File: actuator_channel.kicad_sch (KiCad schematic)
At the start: 1 part

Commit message: исправлены метки
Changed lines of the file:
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@@
 		(instances
 			(project "Untitled"
-				(path "/fcc635d1-682a-4f5e-8a7f-d7e6794df01b"
+				(path "/7d251458-e0b3-4fe3-bf23-623a219baaaa"
 					(reference "U")
 					(unit 1)
@@
 	)
 	(label "GND"
-		(at 48.26 30.48 0)
+		(at 48.26 34.29 270)
 		(effects
 			(font

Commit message: fix writer
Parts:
- removed U: DRV8871 H-мост, symbol Driver_Motor:DRV8871DDA
- added C1, C2: 100nF, symbol Device:C
- added R1: 33k, symbol Device:R
- added R2: 10k, symbol Device:R
- added R3: 20k, symbol Device:R
- added U1: DRV8871 H-мост, symbol Driver_Motor:DRV8871DDA
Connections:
- net FB: now also C2.1, R2.2, R3.1
- net FB_RAW: now also R2.1
- net GND: now also C1.1, C1.2, C2.2, R3.2, U1.1 (GND), U1.5 (VM), U1.7 (GND), U1.9 (GND)
- net IN2: now also U1.2 (IN2)
- new net: R1.1, U1.4 (ILIM)
- new net IN1: U1.3 (IN1)
- new net MOTOR_A: U1.6 (OUT1)
- new net MOTOR_B: U1.8 (OUT2)

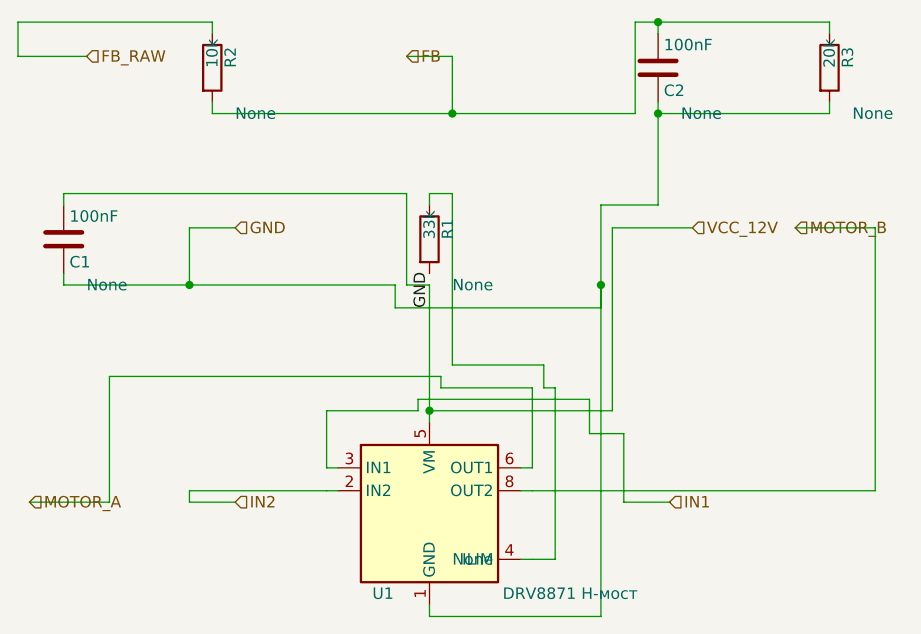
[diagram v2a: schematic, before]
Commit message: реализована 2я занятость клетки
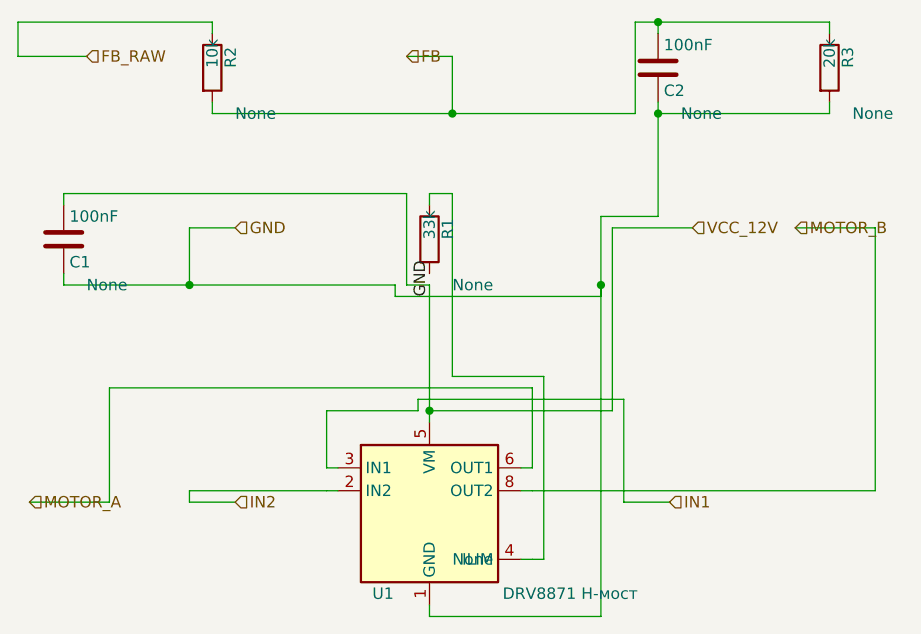
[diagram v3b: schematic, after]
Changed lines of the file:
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@@
 		(instances
 			(project "Untitled"
-				(path "/5363cd59-61ce-4477-bfeb-caaeda29f830"
+				(path "/a4230c37-048a-4d4e-aa82-9745794e2b61"
 					(reference "U1")
 					(unit 1)
@@
 		(instances
 			(project "Untitled"
-				(path "/5363cd59-61ce-4477-bfeb-caaeda29f830"
+				(path "/a4230c37-048a-4d4e-aa82-9745794e2b61"
 					(reference "C1")
 					(unit 1)
@@
 		(instances
 			(project "Untitled"
-				(path "/5363cd59-61ce-4477-bfeb-caaeda29f830"
+				(path "/a4230c37-048a-4d4e-aa82-9745794e2b61"
 					(reference "R1")
 					(unit 1)
@@
 		(instances
 			(project "Untitled"
-				(path "/5363cd59-61ce-4477-bfeb-caaeda29f830"
+				(path "/a4230c37-048a-4d4e-aa82-9745794e2b61"
 					(reference "R2")
 					(unit 1)
@@
 		(instances
 			(project "Untitled"
-				(path "/5363cd59-61ce-4477-bfeb-caaeda29f830"
+				(path "/a4230c37-048a-4d4e-aa82-9745794e2b61"
 					(reference "R3")
 					(unit 1)
@@
 		(instances
 			(project "Untitled"
-				(path "/5363cd59-61ce-4477-bfeb-caaeda29f830"
+				(path "/a4230c37-048a-4d4e-aa82-9745794e2b61"
 					(reference "C2")
 					(unit 1)
@@
 	(wire
 		(pts
-			(xy 67.31 68.58) (xy 67.31 22.86)
-		)
-		(stroke
-			(width 0)
-			(type default)
-		)
-	)
-	(wire
-		(pts
-			(xy 67.31 22.86) (xy 73.66 22.86)
-		)
-		(stroke
-			(width 0)
-			(type default)
-		)
-	)
-	(wire
-		(pts
-			(xy 73.66 22.86) (xy 73.66 12.7)
+			(xy 67.31 68.58) (xy 67.31 24.13)
+		)
+		(stroke
+			(width 0)
+			(type default)
+		)
+	)
+	(wire
+		(pts
+			(xy 67.31 24.13) (xy 73.66 24.13)
+		)
+		(stroke
+			(width 0)
+			(type default)
+		)
+	)
+	(wire
+		(pts
+			(xy 73.66 24.13) (xy 73.66 12.7)
 		)
 		(stroke
@@
 	(wire
 		(pts
-			(xy 44.45 31.75) (xy 44.45 34.29)
-		)
-		(stroke
-			(width 0)
-			(type default)
-		)
-	)
-	(wire
-		(pts
-			(xy 44.45 34.29) (xy 67.31 34.29)
-		)
-		(stroke
-			(width 0)
-			(type default)
-		)
-	)
-	(wire
-		(pts
-			(xy 67.31 34.29) (xy 67.31 31.75)
+			(xy 44.45 31.75) (xy 44.45 33.02)
+		)
+		(stroke
+			(width 0)
+			(type default)
+		)
+	)
+	(wire
+		(pts
+			(xy 44.45 33.02) (xy 67.31 33.02)
+		)
+		(stroke
+			(width 0)
+			(type default)
+		)
+	)
+	(wire
+		(pts
+			(xy 67.31 33.02) (xy 67.31 31.75)
 		)
 		(stroke
@@
 	(wire
 		(pts
-			(xy 46.99 44.45) (xy 66.04 44.45)
-		)
-		(stroke
-			(width 0)
-			(type default)
-		)
-	)
-	(wire
-		(pts
-			(xy 66.04 44.45) (xy 66.04 48.26)
-		)
-		(stroke
-			(width 0)
-			(type default)
-		)
-	)
-	(wire
-		(pts
-			(xy 66.04 48.26) (xy 69.85 48.26)
-		)
-		(stroke
-			(width 0)
-			(type default)
-		)
-	)
-	(wire
-		(pts
-			(xy 69.85 48.26) (xy 69.85 55.88)
+			(xy 46.99 44.45) (xy 69.85 44.45)
+		)
+		(stroke
+			(width 0)
+			(type default)
+		)
+	)
+	(wire
+		(pts
+			(xy 69.85 44.45) (xy 69.85 55.88)
 		)
 		(stroke
@@
 	(wire
 		(pts
-			(xy 59.69 43.18) (xy 49.53 43.18)
-		)
-		(stroke
-			(width 0)
-			(type default)
-		)
-	)
-	(wire
-		(pts
-			(xy 49.53 43.18) (xy 49.53 41.91)
-		)
-		(stroke
-			(width 0)
-			(type default)
-		)
-	)
-	(wire
-		(pts
-			(xy 49.53 41.91) (xy 12.7 41.91)
-		)
-		(stroke
-			(width 0)
-			(type default)
-		)
-	)
-	(wire
-		(pts
-			(xy 12.7 41.91) (xy 12.7 55.88)
+			(xy 59.69 43.18) (xy 12.7 43.18)
+		)
+		(stroke
+			(width 0)
+			(type default)
+		)
+	)
+	(wire
+		(pts
+			(xy 12.7 43.18) (xy 12.7 55.88)
 		)
 		(stroke
@@
 	(wire
 		(pts
-			(xy 59.69 62.23) (xy 62.23 62.23)
-		)
-		(stroke
-			(width 0)
-			(type default)
-		)
-	)
-	(wire
-		(pts
-			(xy 62.23 62.23) (xy 62.23 43.18)
-		)
-		(stroke
-			(width 0)
-			(type default)
-		)
-	)
-	(wire
-		(pts
-			(xy 62.23 43.18) (xy 60.96 43.18)
-		)
-		(stroke
-			(width 0)
-			(type default)
-		)
-	)
-	(wire
-		(pts
-			(xy 60.96 43.18) (xy 60.96 40.64)
-		)
-		(stroke
-			(width 0)
-			(type default)
-		)
-	)
-	(wire
-		(pts
-			(xy 60.96 40.64) (xy 50.8 40.64)
-		)
-		(stroke
-			(width 0)
-			(type default)
-		)
-	)
-	(wire
-		(pts
-			(xy 50.8 40.64) (xy 50.8 21.59)
+			(xy 59.69 62.23) (xy 60.96 62.23)
+		)
+		(stroke
+			(width 0)
+			(type default)
+		)
+	)
+	(wire
+		(pts
+			(xy 60.96 62.23) (xy 60.96 41.91)
+		)
+		(stroke
+			(width 0)
+			(type default)
+		)
+	)
+	(wire
+		(pts
+			(xy 60.96 41.91) (xy 50.8 41.91)
+		)
+		(stroke
+			(width 0)
+			(type default)
+		)
+	)
+	(wire
+		(pts
+			(xy 50.8 41.91) (xy 50.8 21.59)
 		)
 		(stroke
@@
 	)
 	(label "GND"
-		(at 48.26 34.29 270)
+		(at 48.26 33.02 270)
 		(effects
 			(font

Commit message: фильтр клеток для Т если там пересечение
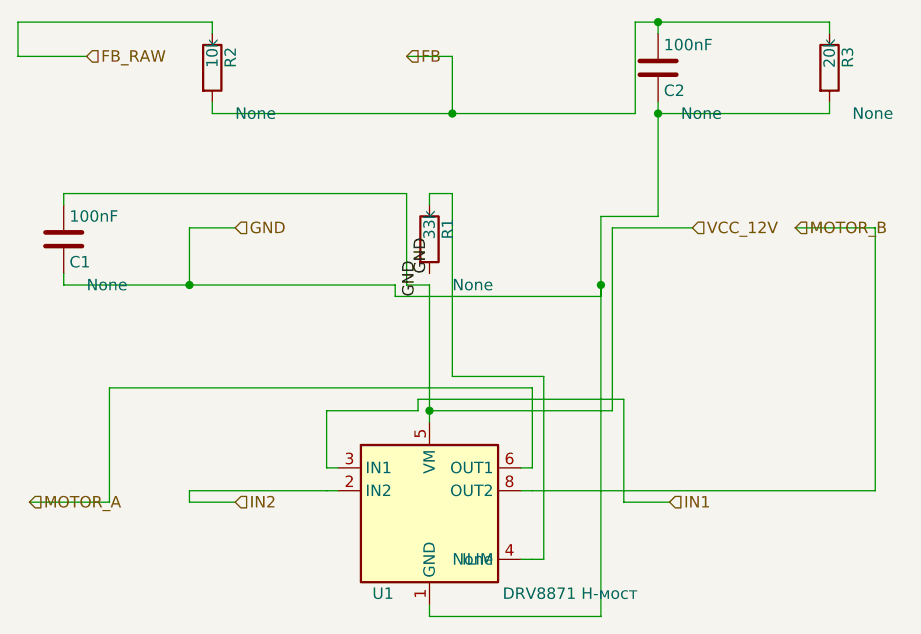
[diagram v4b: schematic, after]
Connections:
- net GND: now also R1.2; no longer C1.1, U1.5 (VM)
- new net VCC_12V: C1.1, U1.5 (VM)
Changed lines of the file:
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@@
 		(instances
 			(project "Untitled"
-				(path "/a4230c37-048a-4d4e-aa82-9745794e2b61"
+				(path "/f13d2b60-b3dd-4fee-9648-3bccc14a03e5"
 					(reference "U1")
 					(unit 1)
@@
 		(instances
 			(project "Untitled"
-				(path "/a4230c37-048a-4d4e-aa82-9745794e2b61"
+				(path "/f13d2b60-b3dd-4fee-9648-3bccc14a03e5"
 					(reference "C1")
 					(unit 1)
@@
 		(instances
 			(project "Untitled"
-				(path "/a4230c37-048a-4d4e-aa82-9745794e2b61"
+				(path "/f13d2b60-b3dd-4fee-9648-3bccc14a03e5"
 					(reference "R1")
 					(unit 1)
@@
 		(instances
 			(project "Untitled"
-				(path "/a4230c37-048a-4d4e-aa82-9745794e2b61"
+				(path "/f13d2b60-b3dd-4fee-9648-3bccc14a03e5"
 					(reference "R2")
 					(unit 1)
@@
 		(instances
 			(project "Untitled"
-				(path "/a4230c37-048a-4d4e-aa82-9745794e2b61"
+				(path "/f13d2b60-b3dd-4fee-9648-3bccc14a03e5"
 					(reference "R3")
 					(unit 1)
@@
 		(instances
 			(project "Untitled"
-				(path "/a4230c37-048a-4d4e-aa82-9745794e2b61"
+				(path "/f13d2b60-b3dd-4fee-9648-3bccc14a03e5"
 					(reference "C2")
 					(unit 1)
@@
 	)
 	(label "GND"
-		(at 48.26 33.02 270)
+		(at 48.26 30.48 270)
 		(effects
 			(font
+				(size 1.27 1.27)
+			)
+			(justify left bottom)
+		)
+	)
+	(label "GND"
+		(at 46.99 33.02 270)
+		(effects
+			(font

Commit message: fic placer for small schemes
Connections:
- net ILIM: now reaches R1.1, U1.4 (ILIM)
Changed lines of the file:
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@@
 		(instances
 			(project "Untitled"
-				(path "/f13d2b60-b3dd-4fee-9648-3bccc14a03e5"
+				(path "/56d967d8-6018-41d7-94fb-71f4db0aa129"
 					(reference "U1")
 					(unit 1)
@@
 		(instances
 			(project "Untitled"
-				(path "/f13d2b60-b3dd-4fee-9648-3bccc14a03e5"
+				(path "/56d967d8-6018-41d7-94fb-71f4db0aa129"
 					(reference "C1")
 					(unit 1)
@@
 		(instances
 			(project "Untitled"
-				(path "/f13d2b60-b3dd-4fee-9648-3bccc14a03e5"
+				(path "/56d967d8-6018-41d7-94fb-71f4db0aa129"
 					(reference "R1")
 					(unit 1)
@@
 		(instances
 			(project "Untitled"
-				(path "/f13d2b60-b3dd-4fee-9648-3bccc14a03e5"
+				(path "/56d967d8-6018-41d7-94fb-71f4db0aa129"
 					(reference "R2")
 					(unit 1)
@@
 		(instances
 			(project "Untitled"
-				(path "/f13d2b60-b3dd-4fee-9648-3bccc14a03e5"
+				(path "/56d967d8-6018-41d7-94fb-71f4db0aa129"
 					(reference "R3")
 					(unit 1)
@@
 		(instances
 			(project "Untitled"
-				(path "/f13d2b60-b3dd-4fee-9648-3bccc14a03e5"
+				(path "/56d967d8-6018-41d7-94fb-71f4db0aa129"
 					(reference "C2")
 					(unit 1)
@@
 		(effects
 			(font
+				(size 1.27 1.27)
+			)
+			(justify left bottom)
+		)
+	)
+	(label "ILIM"
+		(at 60.96 62.23 0.0000)
+		(effects
+			(font

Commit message: all unit test pass
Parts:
- C1, C2: value 100nF -> 100n
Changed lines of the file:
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@@
 		(instances
 			(project "Untitled"
-				(path "/56d967d8-6018-41d7-94fb-71f4db0aa129"
+				(path "/de9cf979-a599-4356-b152-ff3f043da01c"
 					(reference "U1")
 					(unit 1)
@@
 			)
 		)
-		(property "Value" "100nF"
+		(property "Value" "100n"
 			(at 8.255 24.13 0.0000)
 			(effects
@@
 		(instances
 			(project "Untitled"
-				(path "/56d967d8-6018-41d7-94fb-71f4db0aa129"
+				(path "/de9cf979-a599-4356-b152-ff3f043da01c"
 					(reference "C1")
 					(unit 1)
@@
 		(instances
 			(project "Untitled"
-				(path "/56d967d8-6018-41d7-94fb-71f4db0aa129"
+				(path "/de9cf979-a599-4356-b152-ff3f043da01c"
 					(reference "R1")
 					(unit 1)
@@
 		(instances
 			(project "Untitled"
-				(path "/56d967d8-6018-41d7-94fb-71f4db0aa129"
+				(path "/de9cf979-a599-4356-b152-ff3f043da01c"
 					(reference "R2")
 					(unit 1)
@@
 		(instances
 			(project "Untitled"
-				(path "/56d967d8-6018-41d7-94fb-71f4db0aa129"
+				(path "/de9cf979-a599-4356-b152-ff3f043da01c"
 					(reference "R3")
 					(unit 1)
@@
 			)
 		)
-		(property "Value" "100nF"
+		(property "Value" "100n"
 			(at 74.295 5.08 0.0000)
 			(effects
@@
 		(instances
 			(project "Untitled"
-				(path "/56d967d8-6018-41d7-94fb-71f4db0aa129"
+				(path "/de9cf979-a599-4356-b152-ff3f043da01c"
 					(reference "C2")
 					(unit 1)

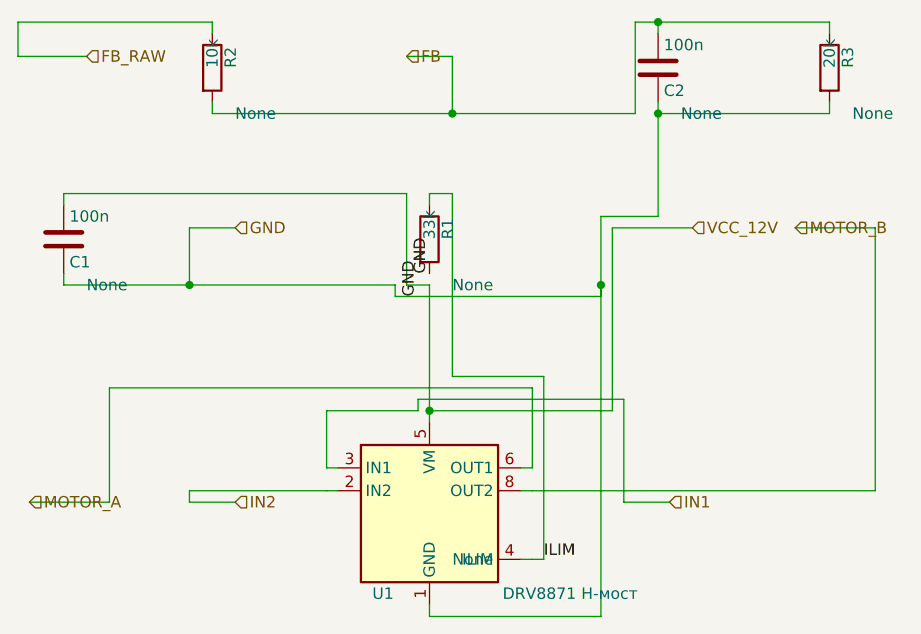
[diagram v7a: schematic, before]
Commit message: optimazed load to kicad
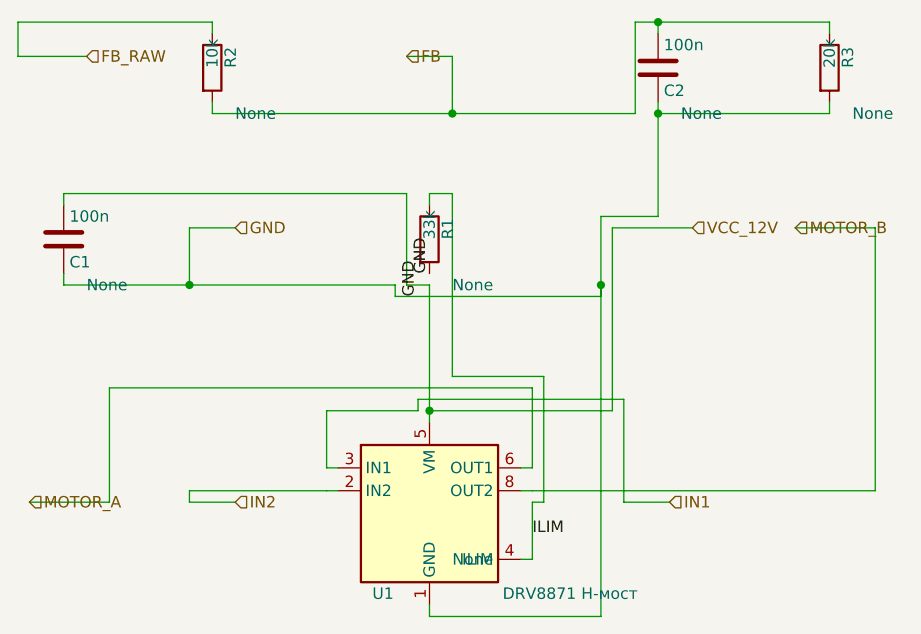
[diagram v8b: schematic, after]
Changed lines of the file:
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@@
 		(instances
 			(project "Untitled"
-				(path "/da0bd840-cf41-4d44-ac31-818f34ecaa1c"
+				(path "/95469d20-8135-4116-bac7-281790b817ac"
 					(reference "U1")
 					(unit 1)
@@
 		(instances
 			(project "Untitled"
-				(path "/da0bd840-cf41-4d44-ac31-818f34ecaa1c"
+				(path "/95469d20-8135-4116-bac7-281790b817ac"
 					(reference "C1")
 					(unit 1)
@@
 		(instances
 			(project "Untitled"
-				(path "/da0bd840-cf41-4d44-ac31-818f34ecaa1c"
+				(path "/95469d20-8135-4116-bac7-281790b817ac"
 					(reference "R1")
 					(unit 1)
@@
 		(instances
 			(project "Untitled"
-				(path "/da0bd840-cf41-4d44-ac31-818f34ecaa1c"
+				(path "/95469d20-8135-4116-bac7-281790b817ac"
 					(reference "R2")
 					(unit 1)
@@
 		(instances
 			(project "Untitled"
-				(path "/da0bd840-cf41-4d44-ac31-818f34ecaa1c"
+				(path "/95469d20-8135-4116-bac7-281790b817ac"
 					(reference "R3")
 					(unit 1)
@@
 		(instances
 			(project "Untitled"
-				(path "/da0bd840-cf41-4d44-ac31-818f34ecaa1c"
+				(path "/95469d20-8135-4116-bac7-281790b817ac"
 					(reference "C2")
 					(unit 1)
@@
 	(wire
 		(pts
-			(xy 59.69 62.23) (xy 60.96 62.23)
-		)
-		(stroke
-			(width 0)
-			(type default)
-		)
-	)
-	(wire
-		(pts
-			(xy 60.96 62.23) (xy 60.96 41.91)
+			(xy 59.69 62.23) (xy 59.69 55.88)
+		)
+		(stroke
+			(width 0)
+			(type default)
+		)
+	)
+	(wire
+		(pts
+			(xy 59.69 55.88) (xy 60.96 55.88)
+		)
+		(stroke
+			(width 0)
+			(type default)
+		)
+	)
+	(wire
+		(pts
+			(xy 60.96 55.88) (xy 60.96 41.91)
 		)
 		(stroke
@@
 	)
 	(label "ILIM"
-		(at 60.96 62.23 0.0000)
+		(at 59.69 59.69 0.0000)
 		(effects
 			(font
